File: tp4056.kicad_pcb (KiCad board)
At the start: 2 copper layers, 43.4 x 20.5 mm, 28 parts, among them J1 Conn_01x01_Pin, J2 Conn_01x01_Female, J3 Conn_01x01_Female, J4 Conn_01x01_Female, J5 Conn_01x01_Female, J6 Conn_01x03_MountingPin, J7 Conn_01x01_Female, J8 USB_C_Receptacle_USB2.0, U1 TP4056, U2 DW01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

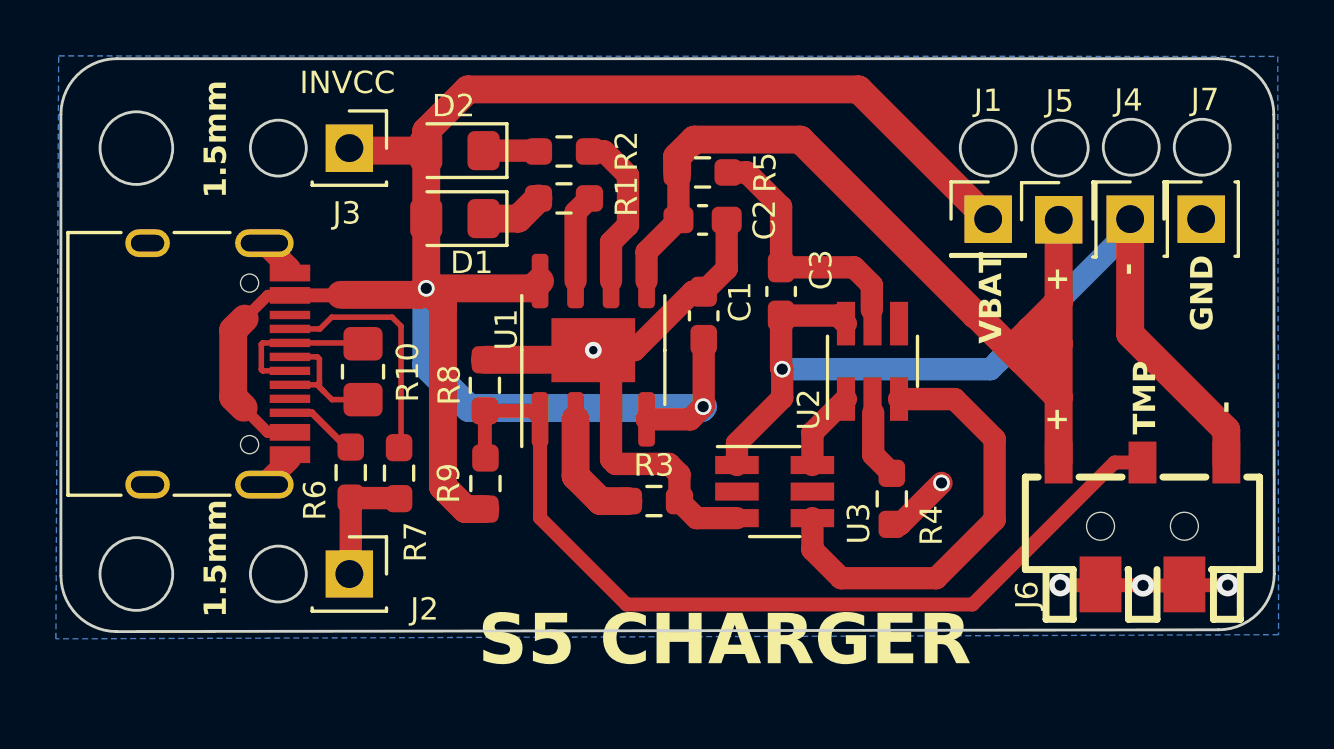
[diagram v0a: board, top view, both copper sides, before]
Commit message: actual changes: moved components around to free some space, added power path outputting on J1, enlarged via under the package to make soldering-iron rework possible, made PROG resistor 0805; designator placement kept reasonable
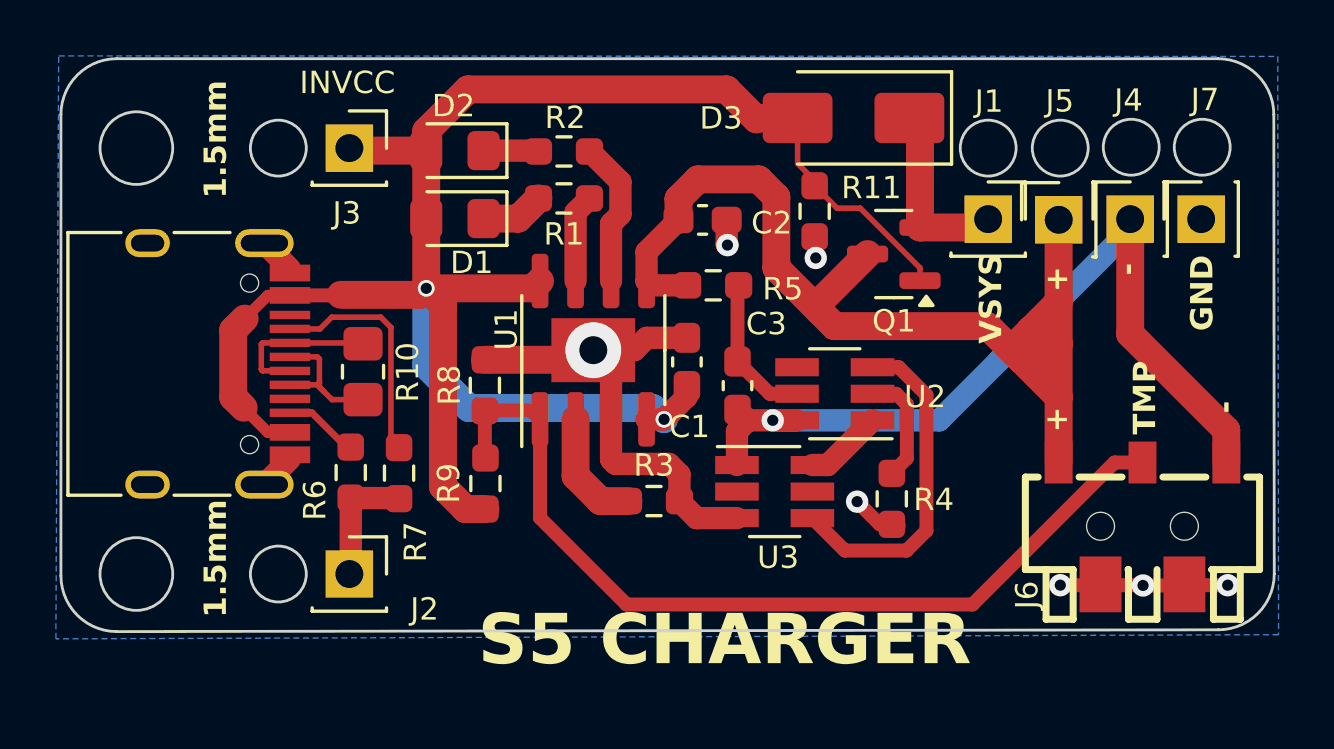
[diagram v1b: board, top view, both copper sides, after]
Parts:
- added D3: SS14, Diode_SMD:D_SMA, F.Cu at (165.4, 75.1)
- added Q1: Q_PMOS_GSD, Package_TO_SOT_SMD:SOT-23, F.Cu at (166.8, 80.0)
- added R11: 2k, Resistor_SMD:R_0603_1608Metric_Pad0.98x0.95mm_HandSolder, F.Cu at (164.0, 78.5)
- J1: footprint Connector_PinHeader_2.54mm:PinHeader_1x01_P2.54mm_Vertical -> Connector_PinSocket_2.54mm:PinSocket_1x01_P2.54mm_Vertical
- moved R5 4.06 mm to (160.3, 81.1)
- moved C3 3.71 mm to (161.2, 84.7)
- moved U2 1.78 mm to (164.7, 85.0), turned to 180 degrees
- moved C1 1.76 mm to (159.4, 83.8)
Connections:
- J1 pad 1: VIN -> /VSYS
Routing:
- net /VSYS: track 0.00 -> 6.64 mm
- net VIN: track 74.9 -> 71.0 mm
- net /G2: track 15.8 -> 12.1 mm
- net BAT+: track 37.1 -> 40.7 mm
- net Net-(U2-VCC): track 8.97 -> 5.35 mm
- net BAT-: track 34.1 -> 30.8 mm
- net GND: track 38.4 -> 35.1 mm, vias 5 -> 7
- net Net-(U2-CS): track 2.44 -> 4.08 mm
- net Net-(U1-~{STDBY}): track 5.75 -> 5.22 mm
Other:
- board text added: "VSYS"
- board text removed: "VBAT"
